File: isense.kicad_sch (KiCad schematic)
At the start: 22 parts

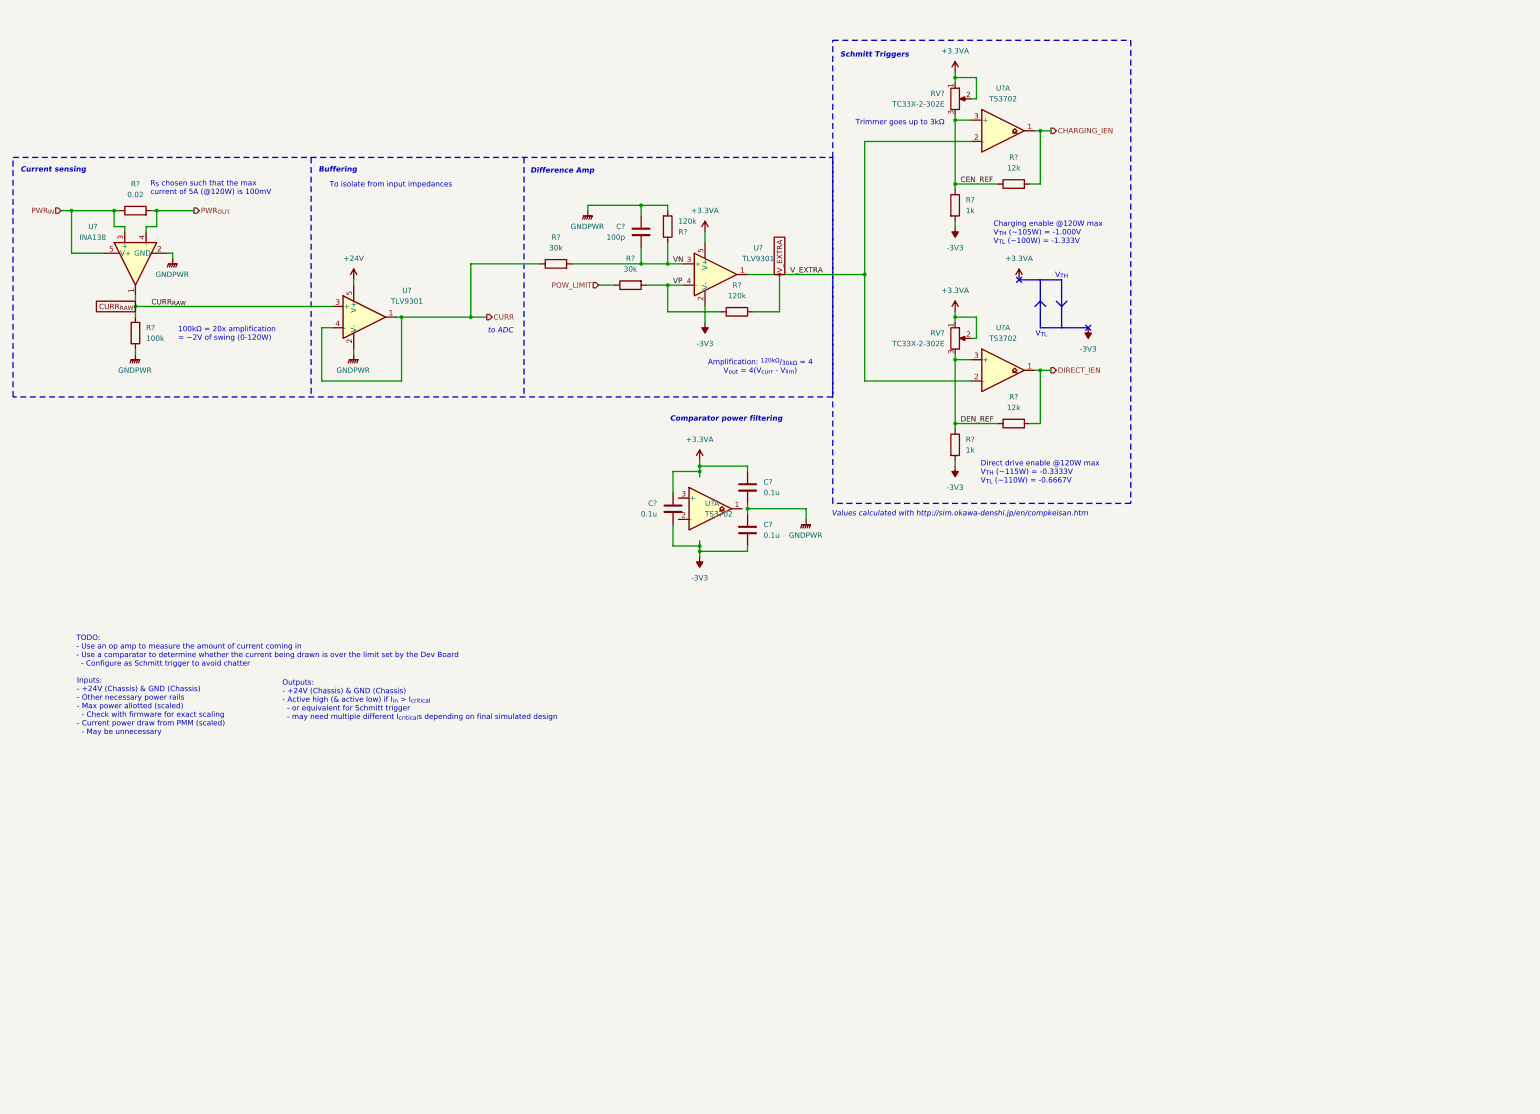
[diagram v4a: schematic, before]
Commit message: Implement SPICE'd circuits in KiCAD
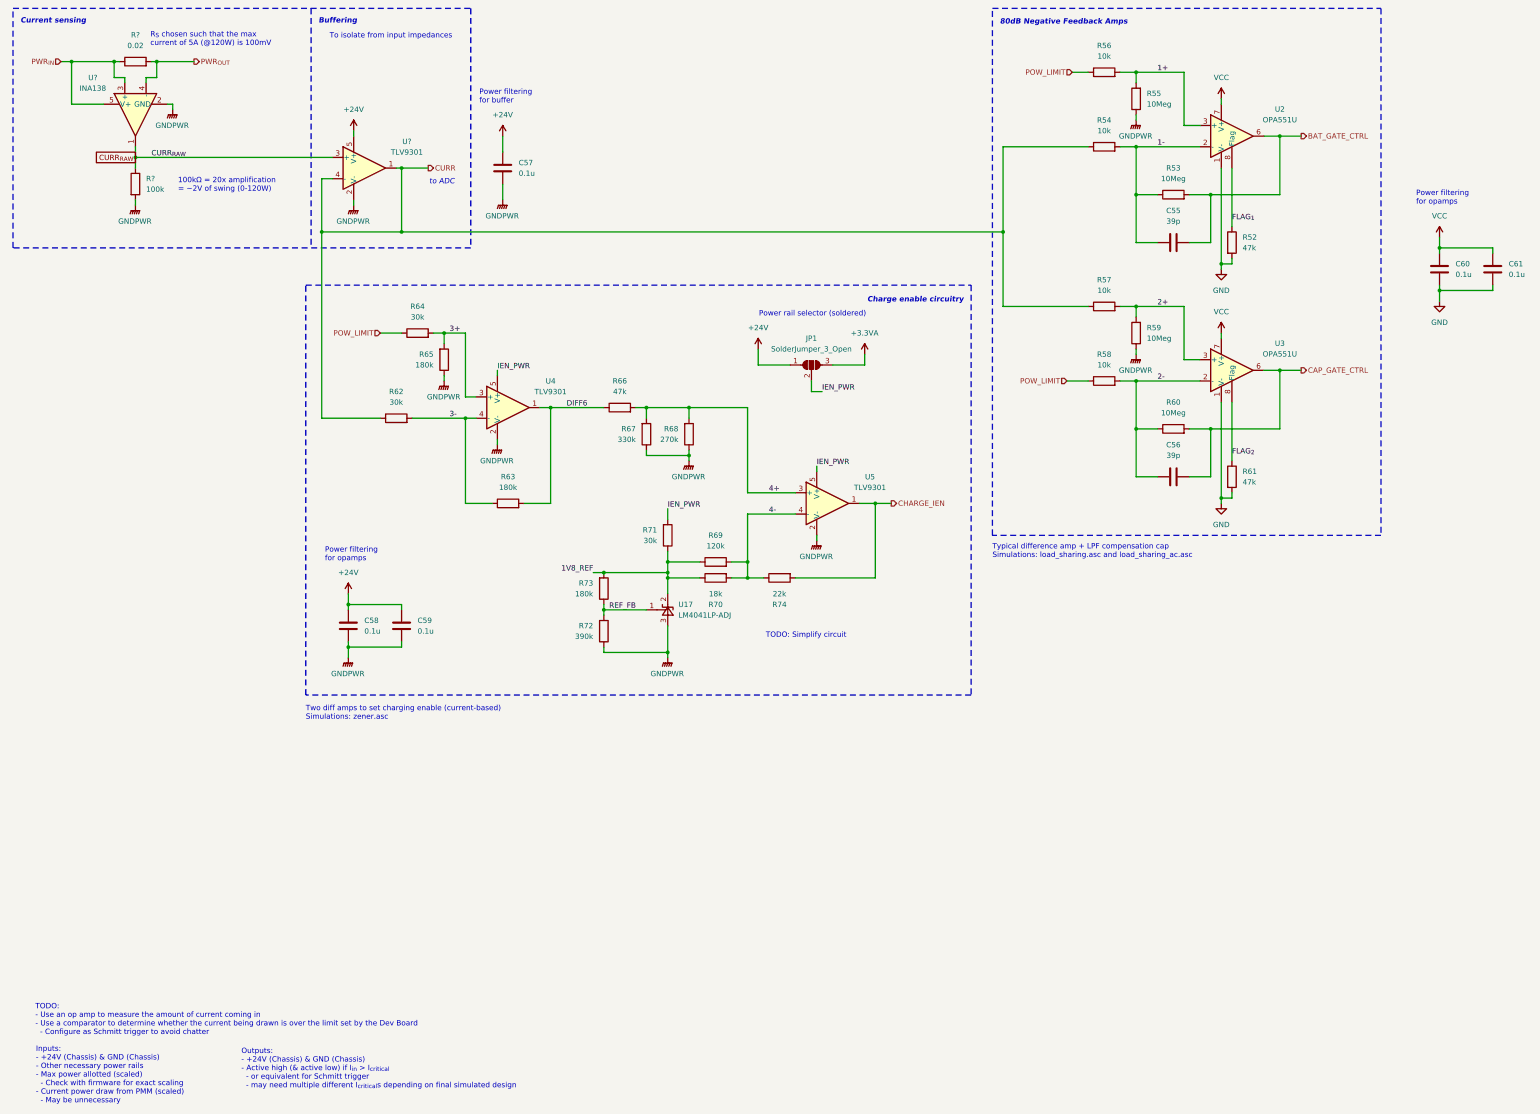
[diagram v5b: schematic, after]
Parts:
- removed C?: 100p, Capacitor_SMD:C_0603_1608Metric_Pad1.08x0.95mm_HandSolder, symbol Device:C
- removed C? (x3): 0.1u, Capacitor_SMD:C_0603_1608Metric_Pad1.08x0.95mm_HandSolder, symbol Device:C
- removed R? (x2): 120k, Resistor_SMD:R_0603_1608Metric_Pad0.98x0.95mm_HandSolder, symbol Device:R
- removed R? (x2): 30k, Resistor_SMD:R_0603_1608Metric_Pad0.98x0.95mm_HandSolder, symbol Device:R
- removed R? (x2): 12k, Resistor_SMD:R_0603_1608Metric_Pad0.98x0.95mm_HandSolder, symbol Device:R
- removed R? (x2): 1k, Resistor_SMD:R_0603_1608Metric_Pad0.98x0.95mm_HandSolder, symbol Device:R
- removed RV? (x2): TC33X-2-302E, Potentiometer_SMD:Potentiometer_Bourns_TC33X_Vertical, symbol Device:R_Potentiometer
- removed U? (x3): TS3702, Package_SO:SOIC-8_3.9x4.9mm_P1.27mm, symbol ! Robomaster ICs:TS3902
- removed U?: TLV9301, Package_TO_SOT_SMD:SOT-23-5_HandSoldering, symbol Amplifier_Operational:LM321
- added C55, C56: 39p, Capacitor_SMD:C_0603_1608Metric_Pad1.08x0.95mm_HandSolder, symbol Device:C
- added C57, C58, C59, C60, C61: 0.1u, Capacitor_SMD:C_0603_1608Metric_Pad1.08x0.95mm_HandSolder, symbol Device:C
- added JP1: SolderJumper_3_Open, Jumper:SolderJumper-3_P1.3mm_Open_RoundedPad1.0x1.5mm, symbol Jumper:SolderJumper_3_Open
- added R52, R61, R66: 47k, Resistor_SMD:R_0603_1608Metric_Pad0.98x0.95mm_HandSolder, symbol Device:R
- added R53, R55, R59, R60: 10Meg, Resistor_SMD:R_0603_1608Metric_Pad0.98x0.95mm_HandSolder, symbol Device:R
- added R54, R56, R57, R58: 10k, Resistor_SMD:R_0603_1608Metric_Pad0.98x0.95mm_HandSolder, symbol Device:R
- added R62, R64, R71: 30k, Resistor_SMD:R_0603_1608Metric_Pad0.98x0.95mm_HandSolder, symbol Device:R
- added R63, R65, R73: 180k, Resistor_SMD:R_0603_1608Metric_Pad0.98x0.95mm_HandSolder, symbol Device:R
- added R67: 330k, Resistor_SMD:R_0603_1608Metric_Pad0.98x0.95mm_HandSolder, symbol Device:R
- added R68: 270k, Resistor_SMD:R_0603_1608Metric_Pad0.98x0.95mm_HandSolder, symbol Device:R
- added R69: 120k, Resistor_SMD:R_0603_1608Metric_Pad0.98x0.95mm_HandSolder, symbol Device:R
- added R70: 18k, Resistor_SMD:R_0603_1608Metric_Pad0.98x0.95mm_HandSolder, symbol Device:R
- added R72: 390k, Resistor_SMD:R_0603_1608Metric_Pad0.98x0.95mm_HandSolder, symbol Device:R
- added R74: 22k, Resistor_SMD:R_0603_1608Metric_Pad0.98x0.95mm_HandSolder, symbol Device:R
- added U17: LM4041LP-ADJ, Package_TO_SOT_THT:TO-92_Inline, symbol Reference_Voltage:LM4041LP-ADJ
- added U2, U3: OPA551U, Package_SO:SOIC-8_3.9x4.9mm_P1.27mm, symbol Amplifier_Operational:OPA551U
- added U4, U5: TLV9301, Package_TO_SOT_SMD:SOT-23-5_HandSoldering, symbol Amplifier_Operational:LM321
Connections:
- net +24V: now also C57.1, C58.1, C59.1, JP1.1 (A)
- net +3.3VA: now also JP1.3 (B)
- net CURR: now also R54.1, R57.1, R62.1
- net GNDPWR: now also C57.2, C58.2, C59.2, R55.1, R59.1, R65.1, R67.1, R68.1, R72.1, U17.3 (A), U4.2 (V-), U5.2 (V-)
- net POW_LIMIT: now also R56.1, R58.1, R64.1
- new net 1+: R55.2, R56.2, U2.3 (+)
- new net 1-: C55.1, R53.1, R54.2, U2.2 (-)
- new net 1V8_REF: R69.1, R70.1, R71.1, R73.2, U17.2 (K)
- new net 2+: R57.2, R59.2, U3.3 (+)
- new net 2-: C56.1, R58.2, R60.1, U3.2 (-)
- new net 3+: R64.2, R65.2, U4.3 (+)
- new net 3-: R62.2, R63.1, U4.4 (-)
- new net 4+: R66.2, R67.2, R68.2, U5.3 (+)
- new net 4-: R69.2, R70.2, R74.1, U5.4 (-)
- new net BAT_GATE_CTRL: C55.2, R53.2, U2.6
- new net CAP_GATE_CTRL: C56.2, R60.2, U3.6
- new net CHARGE_IEN: R74.2, U5.1
- new net DIFF6: R63.2, R66.1, U4.1
- new net FLAG_{1}: R52.1, U2.8 (Flag)
- new net FLAG_{2}: R61.1, U3.8 (Flag)
- new net GND: C60.2, C61.2, R52.2, R61.2, U2.1 (V-), U2.4 (V-), U2.5 (V-), U3.1 (V-), U3.4 (V-), U3.5 (V-)
- new net IEN_PWR: JP1.2 (C), R71.2, U4.5 (V+), U5.5 (V+)
- new net REF_FB: R72.2, R73.1, U17.1 (FB)
- new net VCC: C60.1, C61.1, U2.7 (V+), U3.7 (V+)
- no-connect marks 2 -> 0
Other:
- note added: "80dB Negative Feedback Amps"
- note added: "Charge enable circuitry"
- note added: "Power filtering for buffer"
- note added: "Power filtering for opamps"
- note added: "Power rail selector (soldered)"
- note added: "TODO: Simplify circuit"
- note added: "Two diff amps to set charging enable (current-based) Simulations: zener.asc"
- note added: "Typical difference amp + LPF compensation cap Simulations: load_sharing.asc and load_sharing_ac.asc"
- note removed: "Amplification: ^{120kΩ}/_{30kΩ} = 4 V_{out} = 4(V_{curr} - V_{lim})"
- note removed: "Charging enable @120W max V_{TH} (~105W) = -1.000V V_{TL} (~100W) = -1.333V"
- note removed: "Comparator power filtering"
- note removed: "Difference Amp"
- note removed: "Direct drive enable @120W max V_{TH} (~115W) = -0.3333V V_{TL} (~110W) = -0.6667V"
- note removed: "Schmitt Triggers"
- note removed: "Trimmer goes up to 3kΩ"
- note removed: "V_{TH}"
- note removed: "V_{TL}"
- note removed: "Values calculated with http://sim.okawa-denshi.jp/en/compkeisan.htm"
- moved on the sheet: R?, U?

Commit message: Forgot one label
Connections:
- net +24V: no longer C58.1, C59.1
- net IEN_PWR: now also C58.1, C59.1
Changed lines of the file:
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@@
+		)
+	)
+	(label "IEN_PWR"
+		(at 95.25 156.21 0)
+		(effects
+			(font
+				(size 1.27 1.27)
+			)
+			(justify left bottom)
 		)
 	)
@@
 					(unit 1)
 				)
-			)
-		)
-	)
-	(symbol
-		(lib_id "power:+24V")
-		(at 95.25 156.21 0)
-		(unit 1)
-		(exclude_from_sim no)
-		(in_bom yes)
-		(on_board yes)
-		(dnp no)
-		(fields_autoplaced yes)
-		(property "Reference" "#PWR091"
-			(at 95.25 160.02 0)
-			(effects
-				(font
-					(size 1.27 1.27)
-				)
-				(hide yes)
-			)
-		)
-		(property "Value" "+24V"
-			(at 95.25 151.13 0)
-			(effects
-				(font
-					(size 1.27 1.27)
-				)
-			)
-		)
-		(property "Footprint" ""
-			(at 95.25 156.21 0)
-			(effects
-				(font
-					(size 1.27 1.27)
-				)
-				(hide yes)
-			)
-		)
-		(property "Datasheet" ""
-			(at 95.25 156.21 0)
-			(effects
-				(font
-					(size 1.27 1.27)
-				)
-				(hide yes)
-			)
-		)
-		(property "Description" "Power symbol creates a global label with name \"+24V\""
-			(at 95.25 156.21 0)
-			(effects
-				(font
-					(size 1.27 1.27)
-				)
-				(hide yes)
-			)
-		)
-		(pin "1"
-		)
-		(instances
-			(project "SupercapManager"
-				(path "/6197145b-e7d4-44cc-9d90-537b6501bf60/9739d4cc-938e-4869-b5d8-561f0e1056cb"
-					(reference "#PWR091")
-					(unit 1)
-				)

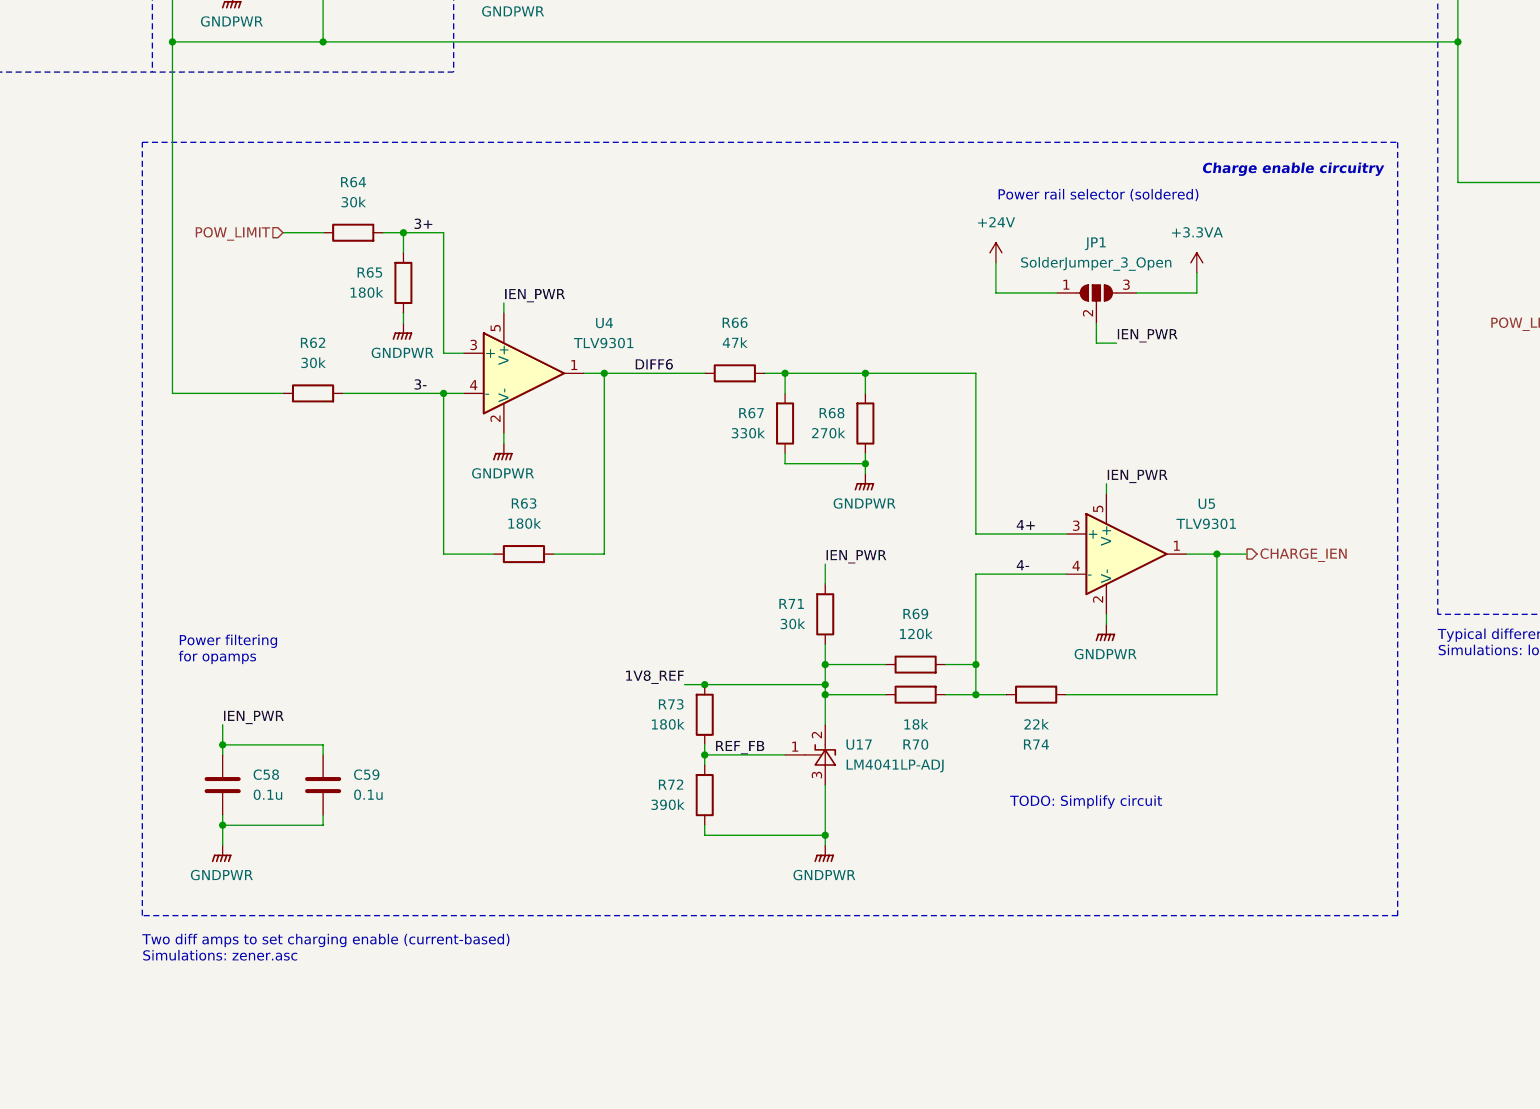
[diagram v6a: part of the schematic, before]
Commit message: Vastly simplified charge EN circuit
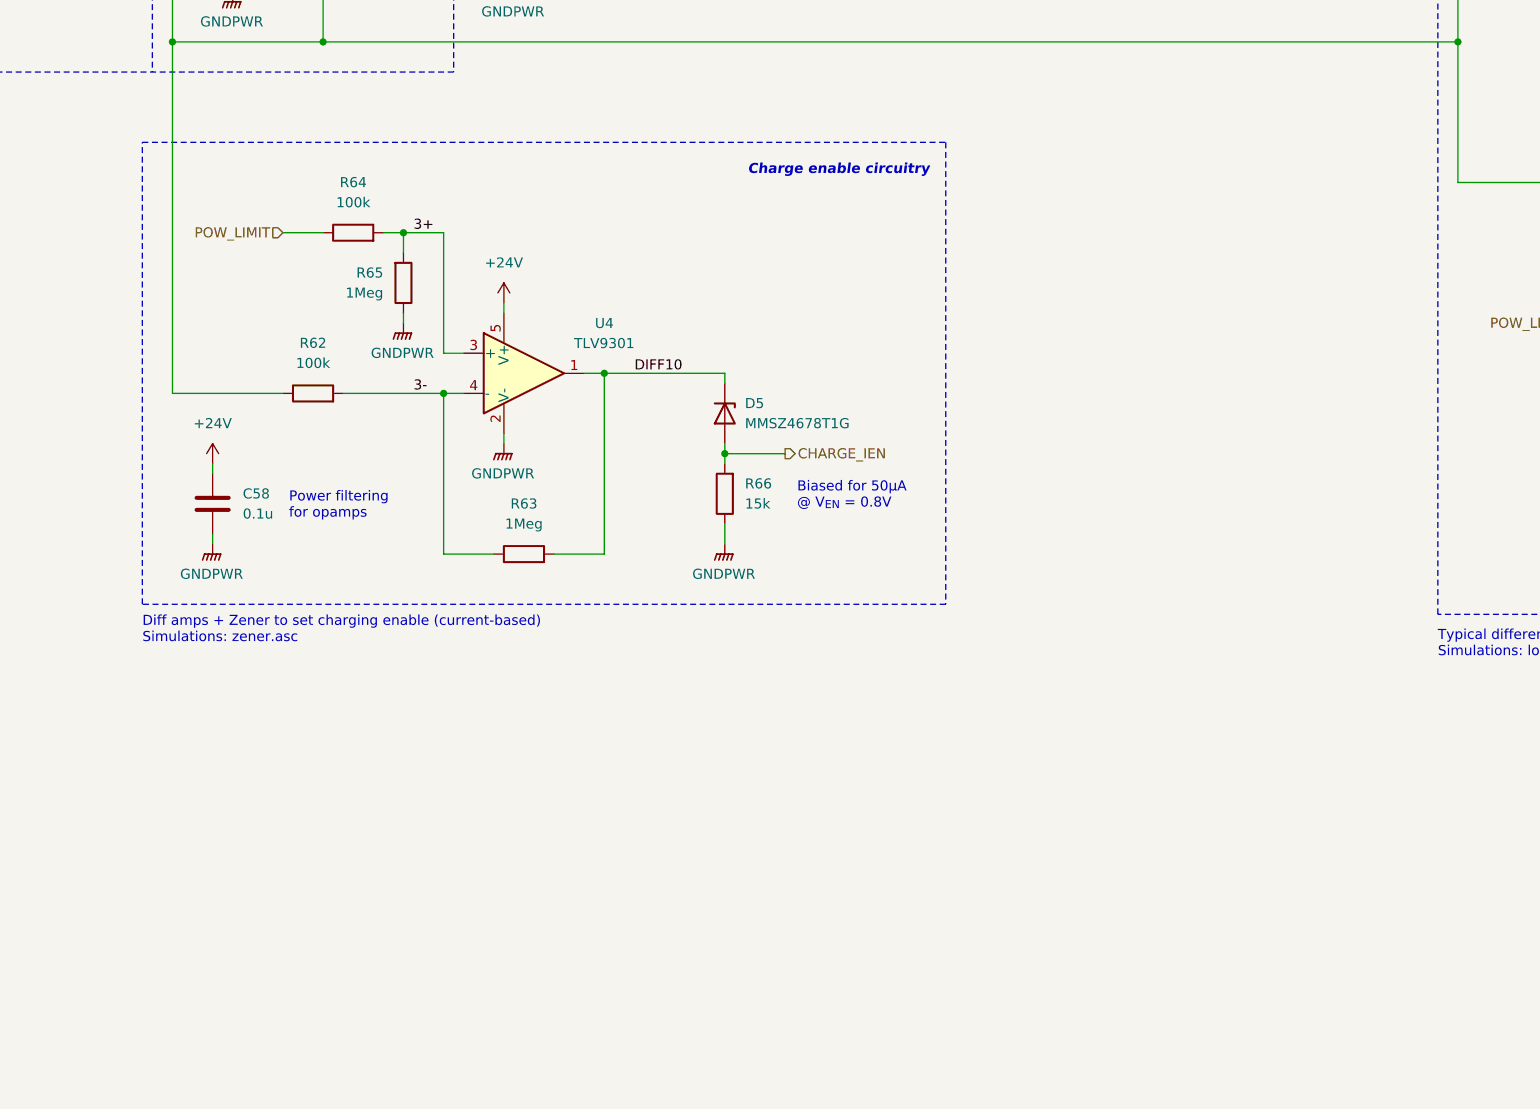
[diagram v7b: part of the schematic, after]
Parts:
- removed C59: 0.1u, Capacitor_SMD:C_0603_1608Metric_Pad1.08x0.95mm_HandSolder, symbol Device:C
- removed JP1: SolderJumper_3_Open, Jumper:SolderJumper-3_P1.3mm_Open_RoundedPad1.0x1.5mm, symbol Jumper:SolderJumper_3_Open
- removed R67: 330k, Resistor_SMD:R_0603_1608Metric_Pad0.98x0.95mm_HandSolder, symbol Device:R
- removed R68: 270k, Resistor_SMD:R_0603_1608Metric_Pad0.98x0.95mm_HandSolder, symbol Device:R
- removed R69: 120k, Resistor_SMD:R_0603_1608Metric_Pad0.98x0.95mm_HandSolder, symbol Device:R
- removed R70: 18k, Resistor_SMD:R_0603_1608Metric_Pad0.98x0.95mm_HandSolder, symbol Device:R
- removed R71: 30k, Resistor_SMD:R_0603_1608Metric_Pad0.98x0.95mm_HandSolder, symbol Device:R
- removed R72: 390k, Resistor_SMD:R_0603_1608Metric_Pad0.98x0.95mm_HandSolder, symbol Device:R
- removed R73: 180k, Resistor_SMD:R_0603_1608Metric_Pad0.98x0.95mm_HandSolder, symbol Device:R
- removed R74: 22k, Resistor_SMD:R_0603_1608Metric_Pad0.98x0.95mm_HandSolder, symbol Device:R
- removed U17: LM4041LP-ADJ, Package_TO_SOT_THT:TO-92_Inline, symbol Reference_Voltage:LM4041LP-ADJ
- removed U5: TLV9301, Package_TO_SOT_SMD:SOT-23-5_HandSoldering, symbol Amplifier_Operational:LM321
- added D5: MMSZ4678T1G, Diode_SMD:D_SOD-123, symbol Device:D_Zener
- R62, R64: value 30k -> 100k
- R63, R65: value 180k -> 1Meg
- R66: value 47k -> 15k
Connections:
- net 4+ is gone; now on net CHARGE_IEN: R66.2
- net IEN_PWR is gone; now on net +24V: C58.1, U4.5 (V+)
- net CHARGE_IEN: now also D5.2 (A)
- net GNDPWR: now also R66.1
- net DIFF6 renamed DIFF10
- net DIFF10: now also D5.1 (K); no longer R66.1
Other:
- note added: "Biased for 50µA @ V_{EN} = 0.8V"
- note added: "Diff amps + Zener to set charging enable (current-based) Simulations: zener.asc"
- note removed: "Power rail selector (soldered)"
- note removed: "TODO: Simplify circuit"
- note removed: "Two diff amps to set charging enable (current-based) Simulations: zener.asc"
- moved on the sheet: C58

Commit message: Redesign housekeeping supplies
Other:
- moved on the sheet: C55, C56, C60, C61, R52, R53, R54, R55, R56, R57, R58, R59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
